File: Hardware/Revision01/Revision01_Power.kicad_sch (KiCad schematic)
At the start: 21 parts, among them J2 JST-PH, Q1 PMV32UP,215, U11 MIC5365-3.3YD5, U8 MAX1837ETT50+T, U9 WE-TPC_5828

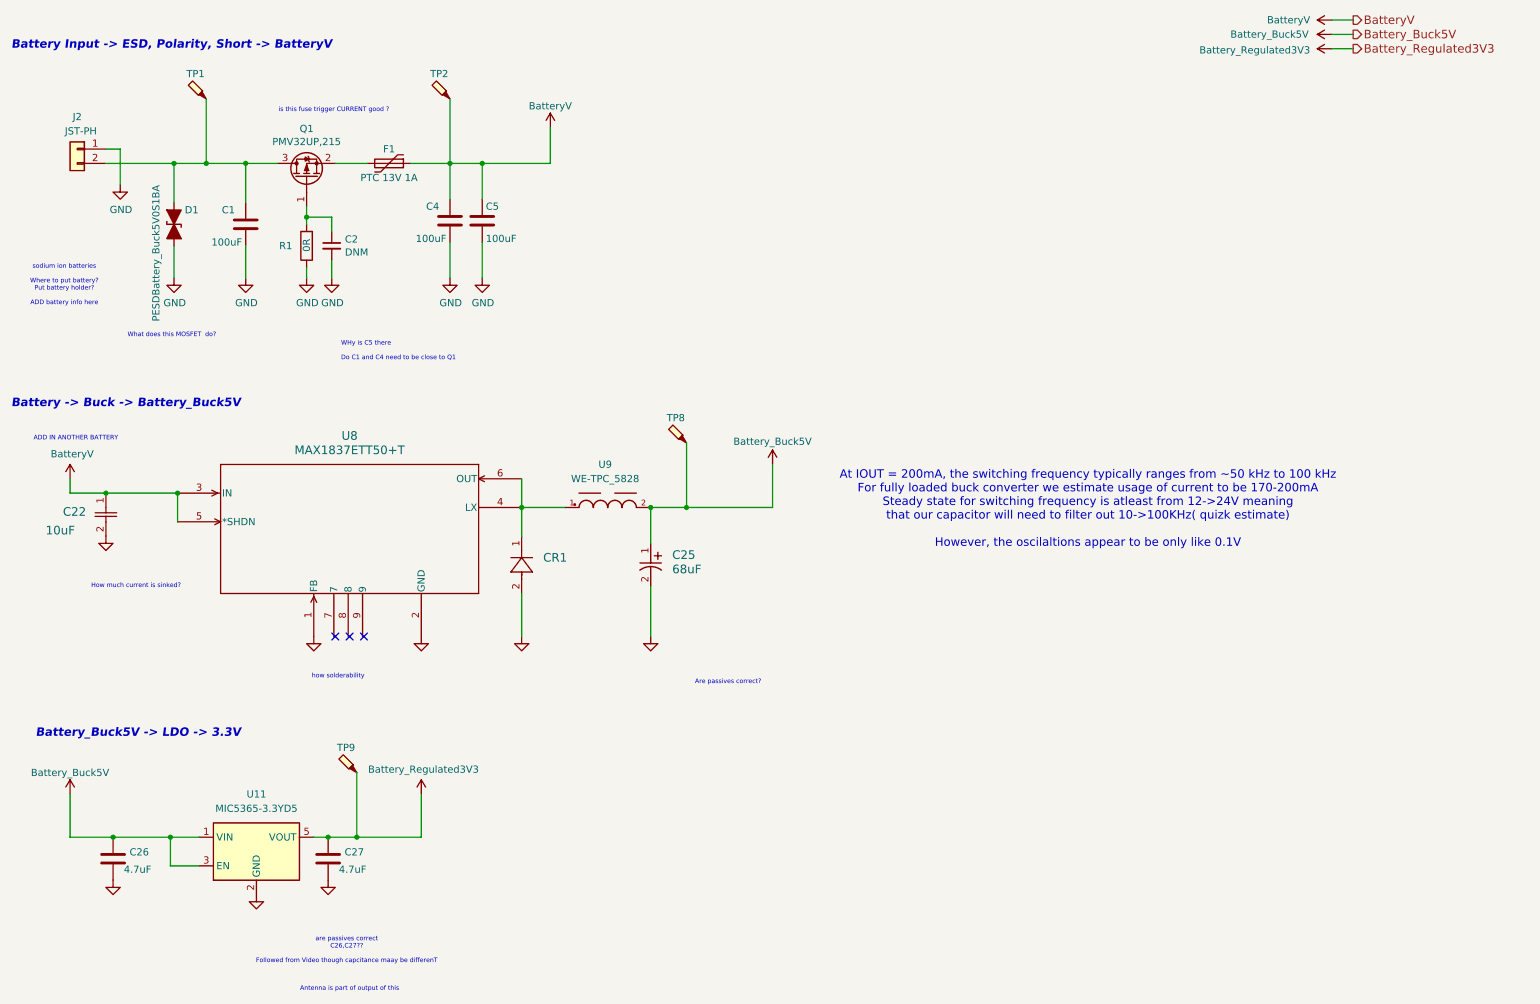
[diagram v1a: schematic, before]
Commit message: . Slight style changes to capacitors, ground symbols; ignored *.swp files
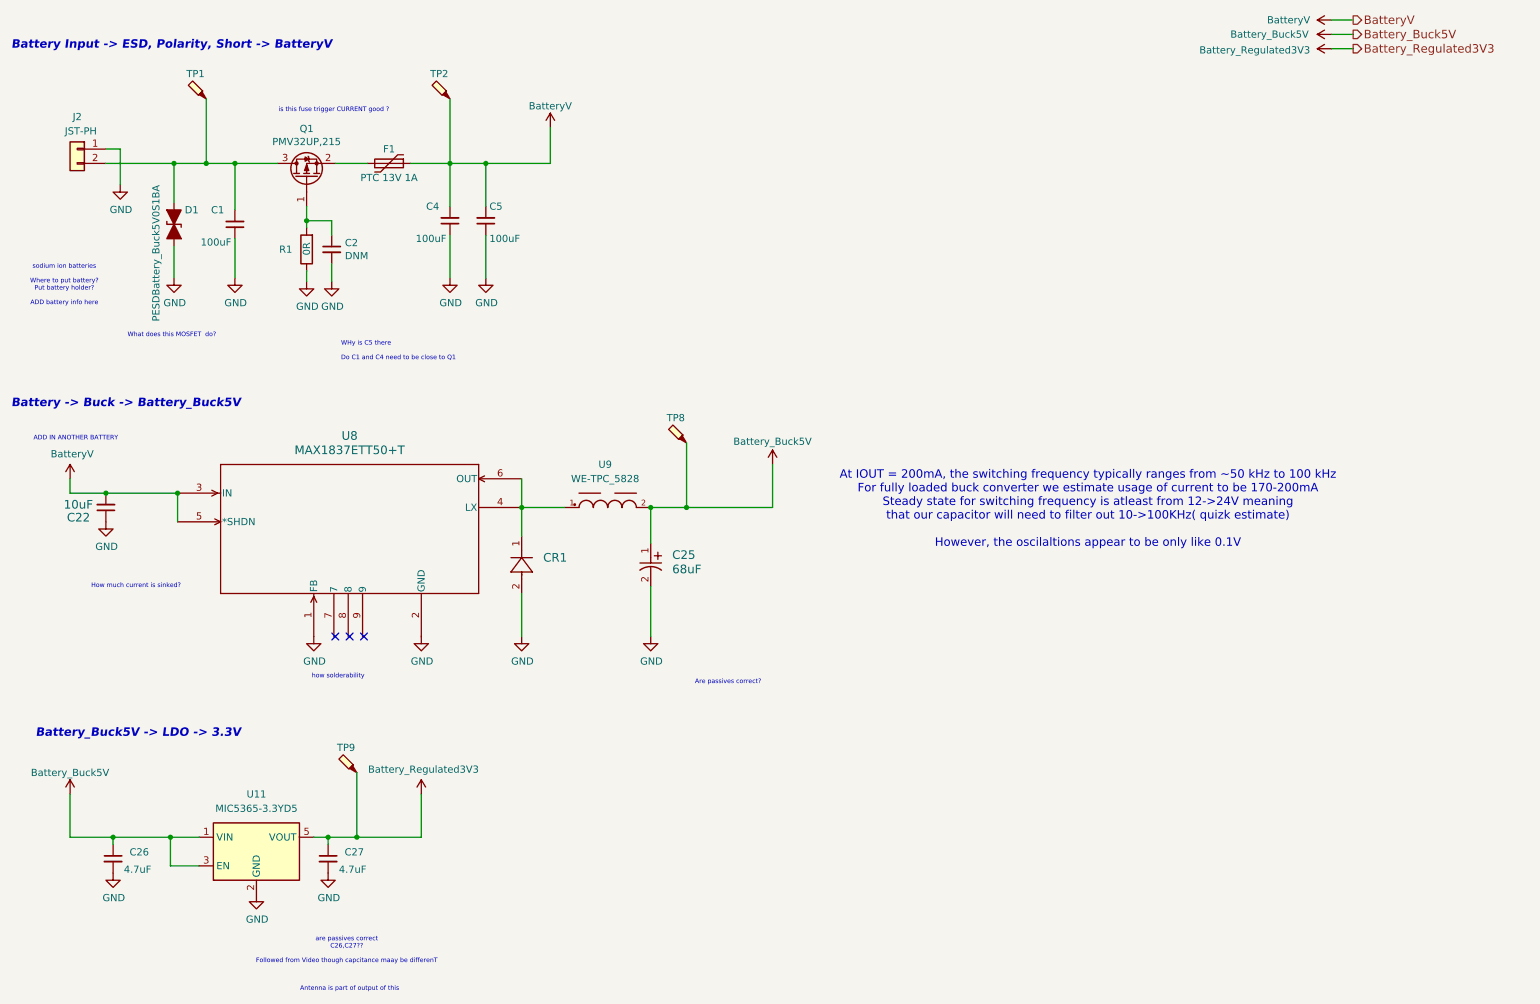
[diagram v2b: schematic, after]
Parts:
- C1, C26, C27, C4, C5: symbol Device:C -> Device:C_Small
- C22: symbol 18123D106KAT2A-10uF-BC:18123D106KAT2A -> Device:C_Small
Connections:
- net BatteryV: now also C22.2; no longer C22.1
- net GND: now also C22.1; no longer C22.2
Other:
- moved on the sheet: C1, C2, C5, R1
